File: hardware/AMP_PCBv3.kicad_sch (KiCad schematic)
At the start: 51 parts, among them CN1 Male_L1, CN2 Male_R2, J1 Input_PWR, J2 VESC_PPM, J3 VESC_COMM, J4 LED_Header, J6 STEERING, M1 Fan_PC_3pin, M3 Fan_PC_3pin, M4 Fan_PC_3pin, M5 Fan_PC_3pin, Q1 DMN2310U, Q2 DMN2310U, Q3 DMN2310U, Q4 DMN2310U, U10 SN74LVC1T45DCK, U11 SN74LVC1T45DCK, U2 AP64500, U7 RFM95W-915S2, U8 SN74LVC1T45DCK, U9 SN74LVC1T45DCK

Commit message: JLC assembly parts
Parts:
- AE1: MPN (none) -> CONSMA001-C-G; now left out of the parts list
- C1: MPN (none) -> CL21B272KBANNNC; now left out of the parts list
- C3, C4, C5: JLC (none) -> C45783
- C8: JLC (none) -> C49678
- C9: JLC (none) -> C15850
- CN1, CN2: now left out of the parts list
- D1, D2, D3: JLC (none) -> C2297
- D10, D11, D4, D9: JLC (none) -> C2128
- D5: JLC (none) -> C84256
- D6, D7, D8: JLC (none) -> C2296
- J1: MPN (none) -> 0039281023; now left out of the parts list
- J2: MPN (none) -> B3B-PH-K-S; now left out of the parts list
- J3: MPN (none) -> B8B-PH-K-S; now left out of the parts list
- J4, M1, M3, M4, M5: MPN (none) -> 0022272031; now left out of the parts list
- J6: MPN (none) -> 0039281083; now left out of the parts list
- L1: footprint Inductor_SMD:L_Changjiang_FNR8040S -> Inductor_SMD:L_Bourns-SRN8040_8x8.15mm; MPN (none) -> SRN8040-3R6Y; now left out of the parts list
- Q1, Q2, Q3, Q4: JLC (none) -> C20917
- R1: JLC (none) -> C17604
- R14, R15, R16, R17, R3: value 260 -> 300; JLC (none) -> C17617
- R2: value 600 -> 470; JLC (none) -> C17710
- R4: MPN (none) -> RK73H2ATTD1582F; now left out of the parts list
- R5: MPN (none) -> RC0805FR-07115KL; now left out of the parts list
- R7: MPN (none) -> RMCF0805FT22K1; now left out of the parts list
- R9: JLC (none) -> C17539
- U10, U11, U8, U9: JLC (none) -> C9382
- U2: JLC (none) -> C2070920
- U7: MPN (none) -> RFM95W-915S2; now left out of the parts list

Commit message: Schematic cleanup
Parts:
- removed AE1: 915MHz, Connector_Coaxial:SMA_Amphenol_132291_Vertical, symbol Device:Antenna_Shield
- removed CN1: Male_L1, Connector_PinHeader_2.54mm:PinHeader_2x19_P2.54mm_Vertical, symbol Connector_Generic:Conn_02x19_Odd_Even
- removed CN2: Male_R2, Connector_PinHeader_2.54mm:PinHeader_2x19_P2.54mm_Vertical, symbol Connector_Generic:Conn_02x19_Odd_Even
- removed D10, D11, D4, D9: D, Diode_SMD:D_SOD-323F, symbol Device:D
- removed D5: STAT4, LED_SMD:LED_0805_2012Metric_Pad1.15x1.40mm_HandSolder, symbol Device:LED_Small
- removed D6: STAT3, LED_SMD:LED_0805_2012Metric_Pad1.15x1.40mm_HandSolder, symbol Device:LED_Small
- removed D7: STAT2, LED_SMD:LED_0805_2012Metric_Pad1.15x1.40mm_HandSolder, symbol Device:LED_Small
- removed D8: STAT1, LED_SMD:LED_0805_2012Metric_Pad1.15x1.40mm_HandSolder, symbol Device:LED_Small
- removed M1, M3, M4, M5: Fan_PC_3pin, Connector_Molex:Molex_KK-254_AE-6410-03A_1x03_P2.54mm_Vertical, symbol AMP_Custom:Fan_PC_3pin
- removed Q1, Q2, Q3, Q4: DMN2310U, Package_TO_SOT_SMD:SOT-23, symbol Transistor_FET:DMN2230U
- removed R14, R15, R16, R17: 300, Resistor_SMD:R_0805_2012Metric_Pad1.20x1.40mm_HandSolder, symbol Device:R_Small_US
- removed U10, U11, U8, U9: SN74LVC1T45DCK, Package_TO_SOT_SMD:SOT-363_SC-70-6, symbol Logic_LevelTranslator:SN74LVC1T45DCK
- removed U7: RFM95W-915S2, RF_Module:HOPERF_RFM9XW_SMD, symbol RF_Module:RFM95W-915S2
- added J5: USB_B_Mini, AMP_Custom:USB_Mini-B_Adam_Tech_MUSB-B5-S-VT-02_Vertical_CircularHoles, symbol Connector:USB_B_Mini
- added M2: Brake, Connector_Molex:Molex_Mini-Fit_Jr_5566-02A_2x01_P4.20mm_Vertical, symbol Motor:Motor_DC
- added U12: ~, AMP_Custom:NUCLEO64, symbol AMP_Custom:NUCLEO64-F446RE
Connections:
- net +3V3: now also U12.16 (+3V3)
- net +5V: now also U12.18 (+5V)
- net BRAKE_CS: now also U12.44 (PC5)
- net BRAKE_INA: now also U12.40 (PC8)
- net BRAKE_INB: now also U12.42 (PC6)
- net BRAKE_PWM: now also U12.43 (PB9)
- net BRAKE_SEL0: now also U12.41 (PB8)
- net GND: now also J5.5 (GND), J5.6 (Shield), U12.19 (GND), U12.20 (GND), U12.22 (GND), U12.47 (GND), U12.58 (GND), U12.8 (GND)
- net IMU_CS: now also U12.71 (PA10)
- net IMU_INT1: now also U12.72 (PC4)
- net LED_SIG: now also U12.62 (PB1)
- net E5V renamed +5P
- net +5P: now also U12.6 (E5V)
- net LED_SIG_5V renamed Status LEDs/LED_SIG_5V
- net PC12 renamed UART5_TX
- net UART5_TX: now also U12.3 (PC12)
- net PC9 renamed VESC_SERVO
- net VESC_SERVO: now also U12.39 (PC9)
- net PD2 renamed UART5_RX
- net UART5_RX: now also U12.4 (PD2)
- new net: U12.10 (NC), U12.11 (NC), U12.26 (NC), U12.48 (NC), U12.56 (NC), U12.74 (NC), U12.76 (NC), U12.9 (NC)
- new net Brake Controller/OUT_A: M2.1 (+)
- new net Brake Controller/OUT_B: M2.2 (-)
- new net FAN1: U12.1 (PC10)
- new net FAN2: U12.2 (PC11)
- new net FAN3: U12.21 (PB7)
- new net FAN4: U12.17 (PA15)
- new net Jetson USB/D+: J5.3 (D+)
- new net Jetson USB/D-: J5.2 (D-)
- new net Jetson USB/VBUS: J5.1 (VBUS)
- new net LORA_DIO0: U12.67 (PB5)
- new net LORA_NSS: U12.68 (PB13)
- new net LORA_RST: U12.65 (PB4)
- new net SPI2_MISO: U12.66 (PB14)
- new net SPI2_MOSI: U12.64 (PB15)
- new net SPI2_SCK: U12.63 (PB10)
- new net STAT1: U12.54 (PB12)
- new net STAT2: U12.52 (PA11)
- new net STAT3: U12.49 (PA5)
- new net STAT4: U12.50 (PA12)
- new net STEERING_ENABLE+_3V3: U12.38 (PC0)
- new net STEERING_INPUT_A+_3V3: U12.36 (PC1)
- new net STEERING_INPUT_A+_DIR: U12.35 (PC2)
- new net STEERING_INPUT_B+_3V3: U12.34 (PB0)
- new net STEERING_INPUT_B+_DIR: U12.32 (PA4)
- new net UART4_RX: U12.30 (PA1)
- new net UART4_TX: U12.28 (PA0)
- no-connect marks 35 -> 26
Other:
- added sheet Fans (Fans.kicad_sch)
- added sheet LoRa (LoRa.kicad_sch)
- added sheet Status LEDs (Status_LEDs.kicad_sch)
- added sheet Steering (Steering.kicad_sch)
- sheet Brake Controller ports: added OUT_A, OUT_B; removed none
- sheet IMU ports: added NSS; removed CS
- sheet Jetson USB ports: added D+, D-, VBUS; removed none
- note added: "5V REGULATOR"
- note added: "CHASSIS FANS"
- note added: "E-BRAKE"
- note added: "IMU"
- note added: "JETSON USB-UART COMMUNICATION"
- note added: "LORA"
- note added: "NUCLEO-64"
- note added: "POWER LEDs"
- note added: "STATUS LEDs"
- note added: "STEERING"
- note added: "STEERING SERVO CONNECTOR"
- note added: "VESC CONNECTORS"
- note removed: "PIN HEADERS"
- moved on the sheet: C1, C3, C4, C5, C8, C9, D1, D2, D3, J1, J2, J3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

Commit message: Final touches for assembly
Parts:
- added H1, H2, H3: Tooling Hole, AMP_Custom:JLCPCB_Tooling_Hole, symbol Mechanical:MountingHole
- U12: now left out of the parts list
- U2: JLCPCB Rotation Offset (none) -> -90
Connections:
- net +5P renamed E5V

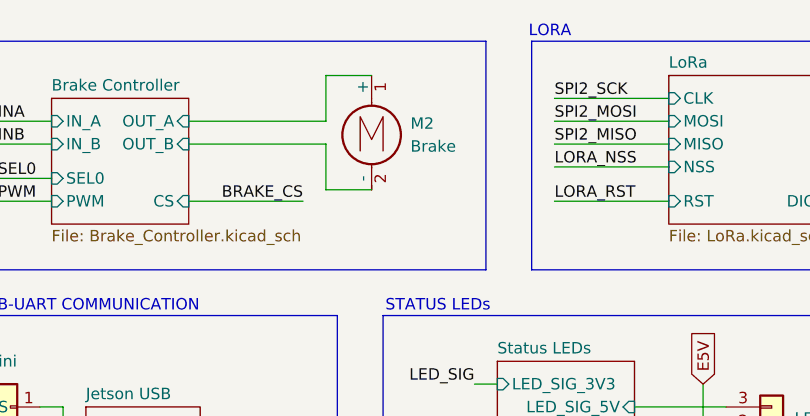
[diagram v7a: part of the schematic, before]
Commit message: Fix #10
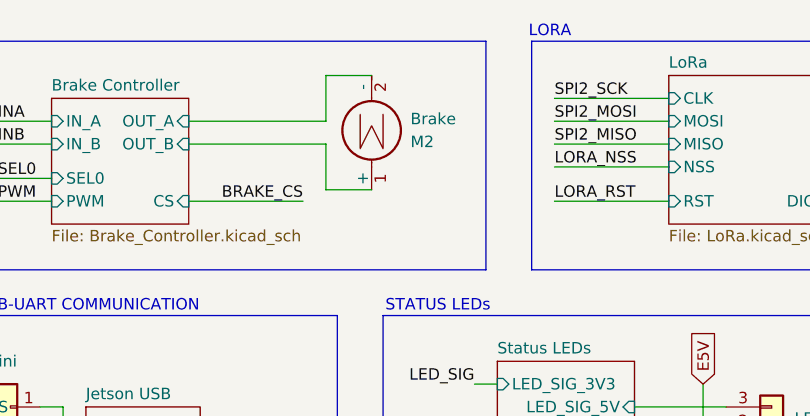
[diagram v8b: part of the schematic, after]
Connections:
- net Brake Controller/OUT_A: now also M2.2 (-); no longer M2.1 (+)
- net Brake Controller/OUT_B: now also M2.1 (+); no longer M2.2 (-)
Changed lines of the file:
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@@
 	(title_block
 		(title "AMP PCBv3")
-		(date "2024-04-14")
-		(rev "C")
+		(date "2024-04-03")
+		(rev "B")
 		(company "Autonomous Motorsports Purdue")
 	)
@@
 	(symbol
 		(lib_id "Motor:Motor_DC")
-		(at 171.45 26.67 0)
+		(at 171.45 29.21 0)
+		(mirror x)
 		(unit 1)
 		(exclude_from_sim no)
@@
 		(dnp no)
 		(property "Reference" "M2"
-			(at 175.768 26.924 0)
+			(at 175.768 28.956 0)
 			(effects
 				(font
@@
 		)
 		(property "Value" "Brake"
-			(at 175.768 29.464 0)
+			(at 175.768 26.416 0)
 			(effects
 				(font
@@
 		)
 		(property "Footprint" "Connector_Molex:Molex_Mini-Fit_Jr_5566-02A_2x01_P4.20mm_Vertical"
-			(at 171.45 28.956 0)
+			(at 171.45 26.924 0)
 			(effects
 				(font
@@
 		)
 		(property "Datasheet" "~"
-			(at 171.45 28.956 0)
+			(at 171.45 26.924 0)
 			(effects
 				(font
@@
 		)
 		(property "Description" ""
-			(at 171.45 26.67 0)
+			(at 171.45 29.21 0)
 			(effects
 				(font
@@
 		)
 		(property "MPN" "0039281023"
-			(at 171.45 26.67 0)
+			(at 171.45 29.21 0)
 			(effects
 				(font
